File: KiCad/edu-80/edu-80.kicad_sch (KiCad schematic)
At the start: 0 parts

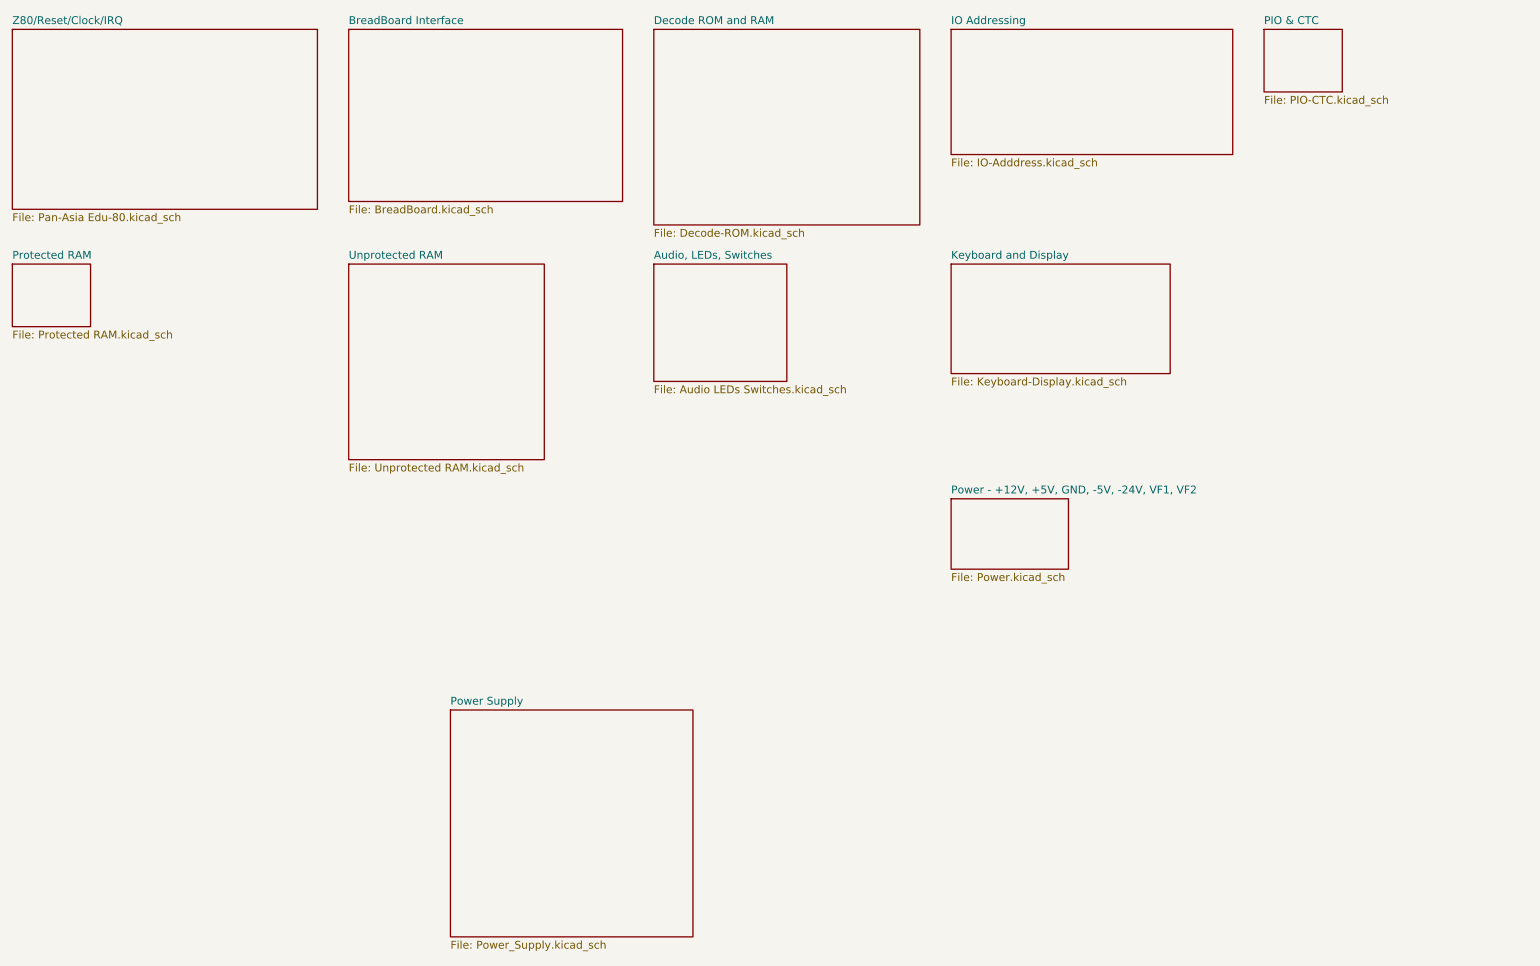
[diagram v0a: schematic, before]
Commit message: Cleaning up the PAL-003 decoding, adding Modifications page.
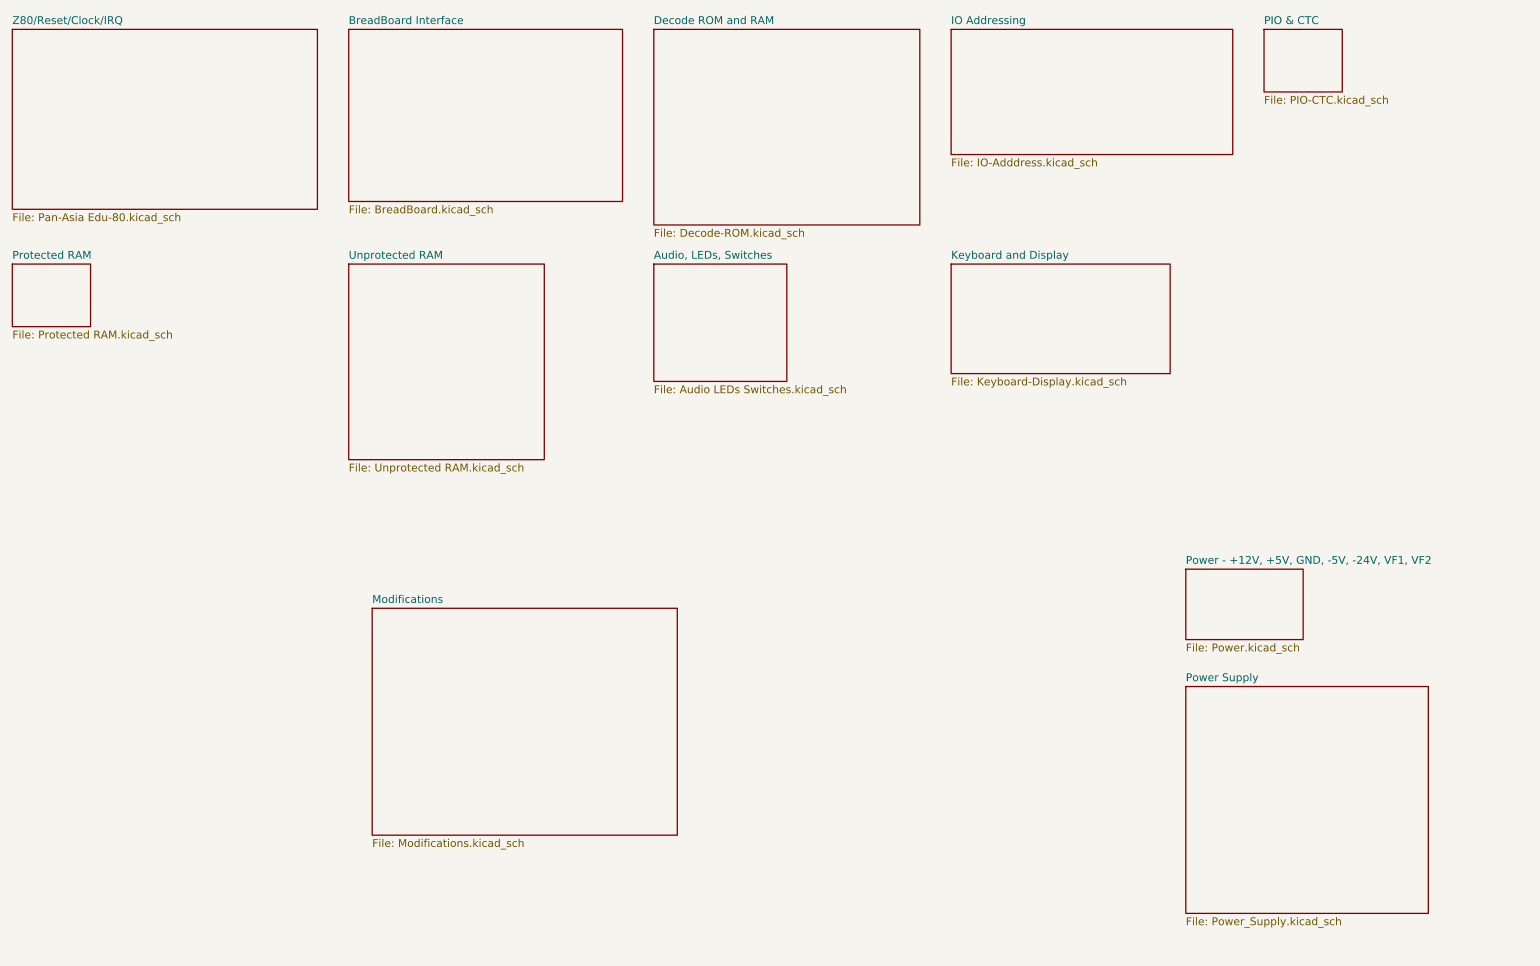
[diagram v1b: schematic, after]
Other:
- added sheet Modifications (Modifications.kicad_sch)
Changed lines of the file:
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@@
   (title_block
     (title "Edu-80 Z80 Trainer")
-    (date "2023-06-01")
+    (date "2023-06-03")
     (rev "0.1")
     (company "Strangers")
+    (comment 1 "Author: James D. Tucker")
   )
   (sheet (at 80.01 25.4) (size 44.45 27.94) (fields_autoplaced)
@@
     )
   )
-  (sheet (at 177.8 101.6) (size 19.05 11.43) (fields_autoplaced)
+  (sheet (at 215.9 113.03) (size 19.05 11.43) (fields_autoplaced)
     (stroke (width 0) (type solid))
     (fill (color 0 0 0 0.0000))
-    (property "Sheetname" "Power - +12V, +5V, GND, -5V, -24V, VF1, VF2" (at 177.8 100.8884 0)
+    (property "Sheetname" "Power - +12V, +5V, GND, -5V, -24V, VF1, VF2" (at 215.9 112.3184 0)
       (effects (font (size 1.27 1.27)) (justify left bottom))
     )
-    (property "Sheetfile" "Power.kicad_sch" (at 177.8 113.6146 0)
+    (property "Sheetfile" "Power.kicad_sch" (at 215.9 125.0446 0)
       (effects (font (size 1.27 1.27)) (justify left top))
     )
@@
     )
   )
-  (sheet (at 96.52 135.89) (size 39.37 36.83) (fields_autoplaced)
+  (sheet (at 83.82 119.38) (size 49.53 36.83) (fields_autoplaced)
     (stroke (width 0.1524) (type solid))
     (fill (color 0 0 0 0.0000))
-    (property "Sheetname" "Power Supply" (at 96.52 135.1784 0)
+    (property "Sheetname" "Modifications" (at 83.82 118.6684 0)
       (effects (font (size 1.27 1.27)) (justify left bottom))
     )
-    (property "Sheetfile" "Power_Supply.kicad_sch" (at 96.52 173.3046 0)
+    (property "Sheetfile" "Modifications.kicad_sch" (at 83.82 156.7946 0)
       (effects (font (size 1.27 1.27)) (justify left top))
     )
+    (instances
+      (project "edu-80"
+        (path "/d19d6db6-a96a-43e3-aa50-c057821f7e22" (page "13"))
+      )
+    )
+  )
+  (sheet (at 215.9 132.08) (size 39.37 36.83) (fields_autoplaced)
+    (stroke (width 0.1524) (type solid))
+    (fill (color 0 0 0 0.0000))
+    (property "Sheetname" "Power Supply" (at 215.9 131.3684 0)
+      (effects (font (size 1.27 1.27)) (justify left bottom))
+    )
+    (property "Sheetfile" "Power_Supply.kicad_sch" (at 215.9 169.4946 0)
+      (effects (font (size 1.27 1.27)) (justify left top))
+    )

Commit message: Adding footprints.
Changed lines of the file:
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@@
     (comment 4 "Author: James D. Tucker")
+  )
+  (text_box "Change the matrix switches to two-terminal footprints."
+    (at 177.8 87.63 0) (size 35.56 8.89)
+    (stroke (width 0) (type default))
+    (fill (type none))
+    (effects (font (face "KiCad Font") (size 1.27 1.27) (thickness 0.254) bold))
   )
   (sheet (at 80.01 25.4) (size 44.45 27.94) (fields_autoplaced)
